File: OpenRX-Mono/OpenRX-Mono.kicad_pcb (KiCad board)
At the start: 6 copper layers, 10 x 14.2 mm, 48 parts, among them T1 0900PC16J0042001E, U1 ESP32-C3FH4, U2 TLV75533PDQNR, U3 TS2306A 240GF MSM 9_C2976675, U4 LR1121IMLTRT, U5 OW7EL89CENUYO3YLC-32M, U7 RFX2401C, U8 SKY13414-485LF, X1 CJ17-400001010B20

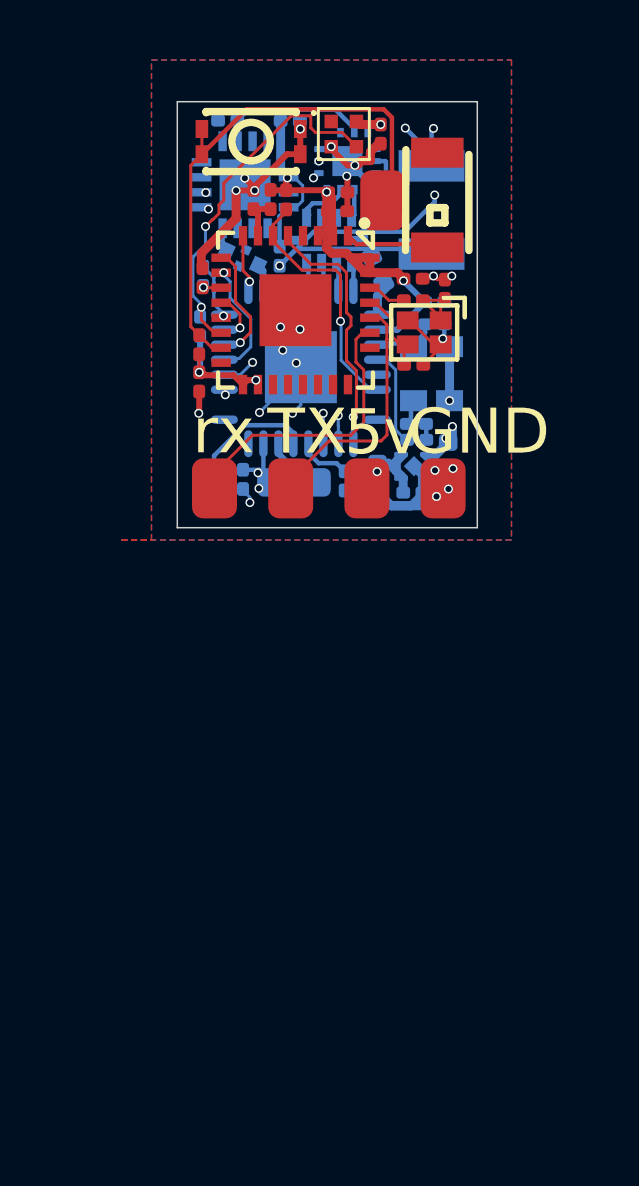
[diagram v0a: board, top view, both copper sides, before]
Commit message: OpenRX Lite (UFL + molex)
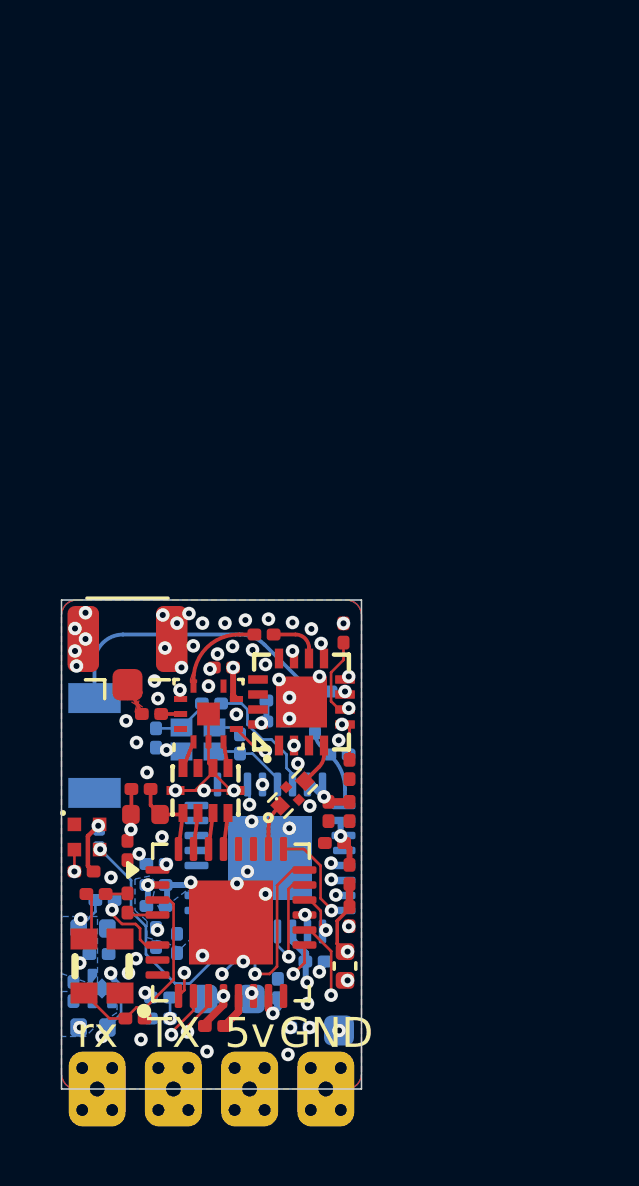
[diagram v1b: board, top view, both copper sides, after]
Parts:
- removed JP1: U.FL-R-SMT-1(80), OpenRX-Shared:RF-SMD_FRF05002-JSS103M
- removed U7: RFX2401C, OpenRX-Shared:QFN-16_L3.0-W3.0-P0.50-BL-EP1.7
- removed U8: SKY13414-485LF, OpenRX-Shared:QFN-14_L2.0-W2.0-P0.45-BL-EP
- added C10: 1uF, Capacitor_SMD:C_0201_0603Metric, B.Cu at (100.4, 113.0)
- added C17: 1uF, Capacitor_SMD:C_0201_0603Metric, B.Cu at (101.2, 111.8)
- added C25: 1uF, Capacitor_SMD:C_0201_0603Metric, F.Cu at (109.1, 108.1)
- added C26: 10nF, Capacitor_SMD:C_0201_0603Metric, F.Cu at (108.9, 107.0)
- added C27: 1uF, Capacitor_SMD:C_0201_0603Metric, B.Cu at (103.2, 111.2)
- added C28: 1uF, Capacitor_SMD:C_0201_0603Metric, B.Cu at (103.3, 114.0)
- added C29: 1.2pF, Capacitor_SMD:C_0201_0603Metric, B.Cu at (109.2, 105.2)
- added C30: 1.2pF, Capacitor_SMD:C_0201_0603Metric, B.Cu at (108.7, 103.0)
- added C31: 1uF, Capacitor_SMD:C_0201_0603Metric, B.Cu at (107.2, 103.3)
- added J1: Conn_Coaxial_Small, Connector_Coaxial:U.FL_Hirose_U.FL-R-SMT-1_Vertical, F.Cu at (102.2, 101.3)
- added L3: 2.0nH, Inductor_SMD:L_0201_0603Metric, F.Cu at (109.6, 109.2)
- added L4: 2.5nH, Inductor_SMD:L_0201_0603Metric, B.Cu at (108.5, 104.1)
- added L5: 47nH, Inductor_SMD:L_0402_1005Metric, F.Cu at (102.8, 107.2)
- added OSC1: OW7EL89CENUYO3YLC-32M, OpenRX-Shared:OSC-SMD_4P-L2.0-W1.6-BL_TXC_7Z, F.Cu at (101.3, 112.2)
- added R7: 100k, Resistor_SMD:R_0201_0603Metric, F.Cu at (109.6, 105.7)
- added R8: 100k, Resistor_SMD:R_0201_0603Metric, F.Cu at (109.4, 101.1)
- AE1, C5, L2, R3, R4, X1: moved to B.Cu
- C1, C3: value 100nF -> 15pF; moved to B.Cu
- C11, FL1, T1: moved to F.Cu
- C12: value 10uF -> 100nF; footprint Capacitor_SMD:C_0402_1005Metric -> Capacitor_SMD:C_0201_0603Metric; moved to F.Cu
- C13: value 10pF -> 100nF; moved to F.Cu
- C14: value 1uF -> 100nF
- C15: value 220pF -> 47pF
- C16: value 0.3pF -> 100nF
- C18: value 100nF -> 10uF; footprint Capacitor_SMD:C_0201_0603Metric -> Capacitor_SMD:C_0402_1005Metric; moved to B.Cu
- C19: value 1uF -> 2.2nF; moved to B.Cu
- C2: value 100nF -> 47p
- C20: value 4.7uF -> 470nF; footprint Capacitor_SMD:C_0402_1005Metric -> Capacitor_SMD:C_0201_0603Metric; moved to F.Cu
- C21: value 100nF -> 220pF
- C22: value 100nF -> 1n; moved to F.Cu
- C23, C24: value 100nF -> 47p; moved to F.Cu
- C4: value 100nF -> 1uF; moved to F.Cu
- C6: value 18pF -> 100nF; moved to B.Cu
- C7: value 18pF -> 10pF
- C8: value 1uF -> 10uF; footprint Capacitor_SMD:C_0201_0603Metric -> Capacitor_SMD:C_0402_1005Metric; moved to B.Cu
- C9: value 1uF -> 100nF; moved to F.Cu
- R1: value 10k -> 200
- R6: value 220R -> 220; moved to F.Cu
- TP5: value Boot -> BOOT; moved to B.Cu
- U1: value ESP32-C3FH4 -> ESP32-C3; footprint OpenRX-Shared:QFN-32_L5.0-W5.0-P0.50-TL-EP3.7 -> Package_DFN_QFN:QFN-32-1EP_5x5mm_P0.5mm_EP3.7x3.7mm; moved to B.Cu
- U3: value TS2306A 240GF MSM 9_C2976675 -> LR1121IMLTRT; footprint OpenRX-Shared:SW-SMD_4P-L3.0-W2.0-P0.85-LS3.5 -> Package_DFN_QFN:QFN-32-1EP_5x5mm_P0.5mm_EP3.7x3.7mm
- U4: value LR1121IMLTRT -> RFX2401C; footprint OpenRX-Shared:QFN-32_L5.0-W5.0-P0.50-BL-EP3.7 -> OpenRX-Shared:QFN-16_L3.0-W3.0-P0.50-BL-EP1.7; moved to F.Cu
- U5: value OW7EL89CENUYO3YLC-32M -> SKY13373-460LF; footprint OpenRX-Shared:OSC-SMD_4P-L2.0-W1.6-BL_TXC_7Z -> OpenRX-Shared:QFN-12_EP_2x2_Pitch0.5mm; moved to F.Cu
- moved C16 29.0 mm to (107.2, 113.0), turned to 90 degrees
- moved C18 28.2 mm to (101.0, 111.0), turned to 0 degrees
- moved C8 28.1 mm to (101.0, 114.2), turned to 0 degrees
- moved TP5 27.7 mm to (109.2, 114.3)
- moved R4 27.6 mm to (108.0, 114.2), turned to 0 degrees
- moved U3 26.0 mm to (105.7, 110.8)
- moved C15 25.9 mm to (103.2, 109.5)
- moved C20 25.8 mm to (105.1, 114.2), turned to 180 degrees
- moved D1 24.9 mm to (100.8, 107.9)
- moved C6 23.6 mm to (103.8, 111.5), turned to -90 degrees
- moved C5 23.1 mm to (108.5, 112.0), turned to 0 degrees
- moved C2 22.4 mm to (102.2, 108.3), turned to -90 degrees
- moved R5 22.4 mm to (103.3, 113.2), turned to 180 degrees
- moved C14 22.0 mm to (103.2, 110.2), turned to 0 degrees
- moved AE1 21.5 mm to (101.1, 104.8), turned to -90 degrees
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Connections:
- C1 pad 1: +3V3 -> Net-(C1-Pad1)
- C12 pad 1: +5V -> +3V3
- C13 pad 1: Net-(C13-Pad1) -> GND
- C13 pad 2: Net-(U4-XTA) -> Net-(OSC1-VDD)
- C16 pad 1: Net-(U7-ANT) -> +3V3
- C18 pad 1: +5V -> +3V3
- C19 pad 1: +3V3 -> /ESP32-C3 + LR1121 Mono/VR_PA
- C2 pad 1: +3V3 -> /ESP32-C3 + LR1121 Mono/VR_PA
- C20 pad 1: Net-(U4-VR_PA) -> GND
- C20 pad 2: GND -> Net-(U3-VREG)
- C22 pad 1: GND -> +3V3
- C22 pad 2: Net-(U4-VREG) -> GND
- C23 pad 1: GND -> Net-(U4-ANT)
- C23 pad 2: Net-(U4-VTCXO) -> Net-(U5-J2)
- C24 pad 1: GND -> Net-(U5-RFC)
- C24 pad 2: +3V3 -> Net-(J1-In)
- C3 pad 1: +3V3 -> /ESP32-C3 + LR1121 Mono/XTAL_N
- C6 pad 1: Net-(C6-Pad1) -> +3V3
- C7 pad 1: /ESP32-C3 + LR1121 Mono/XTAL_N -> Net-(C7-Pad1)
- C7 pad 2: GND -> Net-(OSC1-OutPut)
- C8 pad 1: /ESP32-C3 + LR1121 Mono/CHIP_EN -> +5V
- C9 pad 1: +5V -> +3V3
- D1 pad 2: +5V -> +3V3
- L1 pad 1: Net-(U4-DCC_SW) -> Net-(U3-DCC_SW)
- L1 pad 2: +3V3 -> Net-(U3-VREG)
- L2 pad 1: Net-(C6-Pad1) -> Net-(C1-Pad1)
- R1 pad 1: +3V3 -> /ESP32-C3 + LR1121 Mono/VR_PA
- R1 pad 2: /ESP32-C3 + LR1121 Mono/CHIP_EN -> Net-(T1-RFO_HP_LF)
- R2 pad 2: /ESP32-C3 + LR1121 Mono/NSS1 -> /ESP32-C3 + LR1121 Mono/RST
- R3 pad 2: /ESP32-C3 + LR1121 Mono/BUTTON -> /ESP32-C3 + LR1121 Mono/LED
- R4 pad 2: /ESP32-C3 + LR1121 Mono/RST1 -> /ESP32-C3 + LR1121 Mono/BOOT
- R5 pad 1: +3V3 -> /ESP32-C3 + LR1121 Mono/CHIP_EN
- R5 pad 2: /ESP32-C3 + LR1121 Mono/LED -> +3V3
- R6 pad 1: Net-(C13-Pad1) -> Net-(C7-Pad1)
- R6 pad 2: Net-(U5-OUTPUT) -> Net-(U3-XTA)
- TP5 pad 1: /ESP32-C3 + LR1121 Mono/BUTTON -> /ESP32-C3 + LR1121 Mono/BOOT
- U1 pad 1: /ESP32-C3 + LR1121 Mono/WIFI -> Net-(U1-LNA_IN)
- U1 pad 13: /ESP32-C3 + LR1121 Mono/NSS1 -> /ESP32-C3 + LR1121 Mono/NSS
- U1 pad 15: /ESP32-C3 + LR1121 Mono/BUTTON -> /ESP32-C3 + LR1121 Mono/BOOT
- U1 pad 2: +3V3 -> Net-(C25-Pad1)
- U1 pad 3: +3V3 -> Net-(C25-Pad1)
- U1 pad 5: /ESP32-C3 + LR1121 Mono/IRQ1 -> /ESP32-C3 + LR1121 Mono/DIO1
- U1 pad 6: /ESP32-C3 + LR1121 Mono/RST1 -> /ESP32-C3 + LR1121 Mono/RST
- U1 pad 8: /ESP32-C3 + LR1121 Mono/BUSY1 -> /ESP32-C3 + LR1121 Mono/BUSY
- U3 pad 1: /ESP32-C3 + LR1121 Mono/BUTTON -> /ESP32-C3 + LR1121 Mono/VR_PA
- U3 pad 2: GND -> +3V3
- U4 pad 1: Net-(U4-VR_PA) -> GND
- U4 pad 10: /ESP32-C3 + LR1121 Mono/DIO8-1 -> Net-(U4-ANT)
- U4 pad 11: /ESP32-C3 + LR1121 Mono/DIO7-1 -> GND
- U4 pad 12: Net-(U4-VREG) -> GND
- U4 pad 13: GND -> unconnected-(U4-DNC-Pad13)
- U4 pad 14: Net-(U4-DCC_SW) -> unconnected-(U4-VDD-Pad14)
- U4 pad 15: +3V3 -> GND
- U4 pad 16: unconnected-(U4-DNC-Pad16) -> +3V3
- U4 pad 17: unconnected-(U4-DNC-Pad17) -> GND
- U4 pad 2: +3V3 -> GND
- U4 pad 3: Net-(U4-VTCXO) -> GND
- U4 pad 4: Net-(U4-XTA) -> Net-(FL1-OUT)
- U4 pad 5: unconnected-(U4-XTB-Pad5) -> /ESP32-C3 + LR1121 Mono/TXEN24
- U4 pad 6: /ESP32-C3 + LR1121 Mono/RST1 -> /ESP32-C3 + LR1121 Mono/RXEN24
- U4 pad 8: unconnected-(U4-32k_N/DIO10-Pad8) -> GND
- U4 pad 9: /ESP32-C3 + LR1121 Mono/IRQ1 -> GND
- U5 pad 1: GND -> Net-(T1-TX_HP)
- U5 pad 3: Net-(U5-OUTPUT) -> Net-(T1-RX)
- U5 pad 4: Net-(U4-VTCXO) -> /ESP32-C3 + LR1121 Mono/CTRL1
- X1 pad 1: Net-(C6-Pad1) -> Net-(C1-Pad1)
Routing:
- net GND: track 57.3 -> 14.3 mm, vias 27 -> 66
- net /ESP32-C3 + LR1121 Mono/BUTTON: track 18.2 -> 0.00 mm
- net /ESP32-C3 + LR1121 Mono/CTRL1: track 0.00 -> 17.2 mm, vias 0 -> 3
- net +3V3: track 30.1 -> 14.0 mm, vias 10 -> 14
- net /ESP32-C3 + LR1121 Mono/RXEN24: track 0.00 -> 15.4 mm, vias 0 -> 2
- net /ESP32-C3 + LR1121 Mono/CTRL2: track 0.00 -> 14.2 mm, vias 0 -> 3
- net /ESP32-C3 + LR1121 Mono/TXEN24: track 0.00 -> 12.3 mm, vias 0 -> 2
- net /ESP32-C3 + LR1121 Mono/RST: track 0.00 -> 10.9 mm, vias 0 -> 2
- net /ESP32-C3 + LR1121 Mono/DIO8-1: track 9.95 -> 0.00 mm, vias 2 -> 0
- net /ESP32-C3 + LR1121 Mono/DIO7-1: track 9.25 -> 0.00 mm, vias 2 -> 0
- net /ESP32-C3 + LR1121 Mono/TXEN: track 8.59 -> 0.00 mm, vias 2 -> 0
- net /ESP32-C3 + LR1121 Mono/IRQ1: track 8.57 -> 0.00 mm, vias 1 -> 0
- net +5V: track 15.1 -> 6.64 mm, vias 2 -> 1
- net /ESP32-C3 + LR1121 Mono/RST1: track 8.42 -> 0.00 mm, vias 1 -> 0
- net /ESP32-C3 + LR1121 Mono/DIO1: track 0.00 -> 8.15 mm, vias 0 -> 2
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- added copper zone on B.Cu, net +3V3
- added copper zone on B.Cu, net +5V
- added copper zone on F.Cu, net Net-(J1-In)
- added copper zone on F.Cu, net Net-(U5-J2)
- removed copper zone on In3.Cu, net GND
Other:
- board size 10 x 14.2 mm -> 10 x 16.3 mm
- board text added: "BOOT"
- board text added: "OPEN"
- board text added: "RX"
